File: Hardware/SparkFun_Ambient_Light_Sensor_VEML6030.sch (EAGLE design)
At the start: 25 parts, among them U1 VEML6030

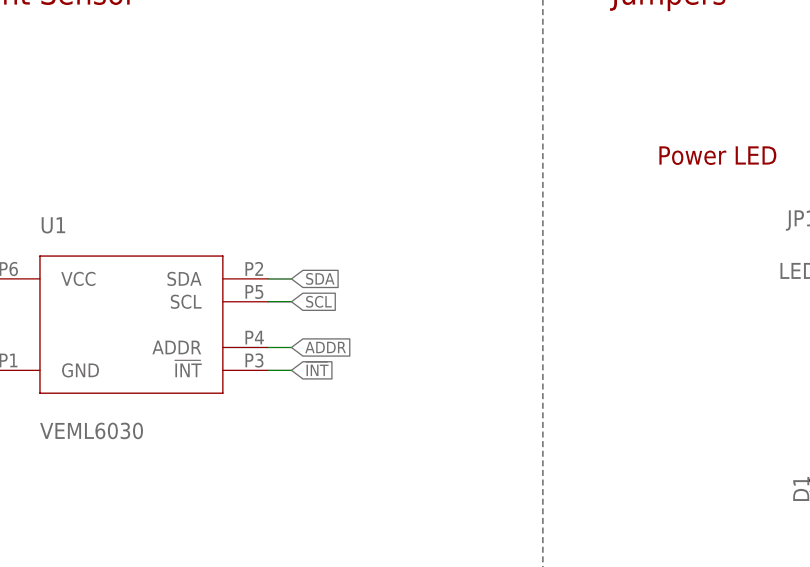
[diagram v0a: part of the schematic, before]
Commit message: Finishes tracework, adds 10k pull up resistor to interrupt pin, needs silk
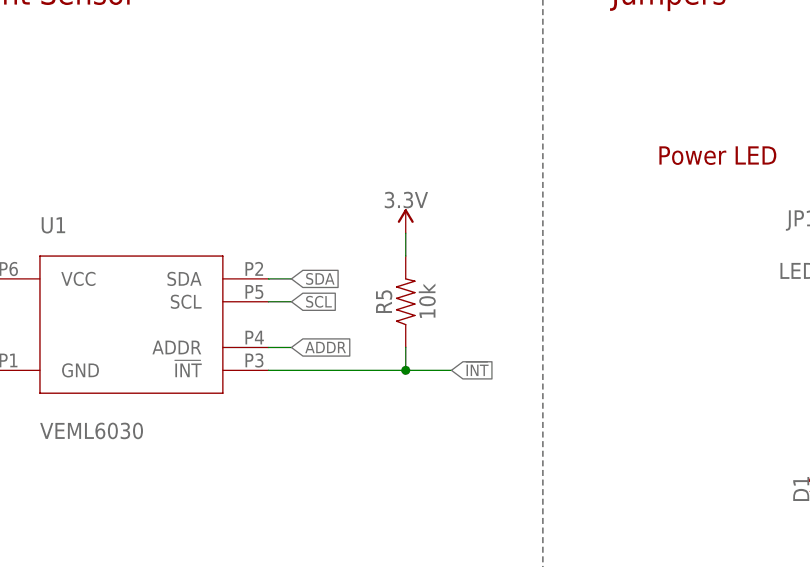
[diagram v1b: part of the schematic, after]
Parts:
- added R5: 10k, SparkFun-Resistors:10KOHM-0603-1/10W-1%
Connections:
- net !INT: now also R5.1
- net 3.3V: now also R5.2
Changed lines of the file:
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@@
 <part name="JP3" library="SparkFun-Jumpers" deviceset="JUMPER-SMT_3_2-NC_TRACE" device="_SILK" value="I2C_PU"/>
 <part name="SUPPLY7" library="SparkFun-PowerSymbols" deviceset="3.3V" device=""/>
+<part name="R5" library="SparkFun-Resistors" deviceset="10KOHM" device="-0603-1/10W-1%" value="10k"/>
+<part name="SUPPLY8" library="SparkFun-PowerSymbols" deviceset="3.3V" device=""/>
 </parts>
 <sheets>
@@
 <attribute name="VALUE" x="193.04" y="124.714" size="1.778" layer="96" align="bottom-center"/>
 </instance>
+<instance part="R5" gate="G$1" x="86.36" y="142.24" smashed="yes" rot="R90">
+<attribute name="NAME" x="84.836" y="142.24" size="1.778" layer="95" font="vector" rot="R90" align="bottom-center"/>
+<attribute name="VALUE" x="87.884" y="142.24" size="1.778" layer="96" font="vector" rot="R90" align="top-center"/>
+</instance>
+<instance part="SUPPLY8" gate="G$1" x="86.36" y="149.86" smashed="yes">
+<attribute name="VALUE" x="86.36" y="152.654" size="1.778" layer="96" align="bottom-center"/>
+</instance>
 </instances>
 <busses>
@@
 <wire x1="132.08" y1="83.82" x2="132.08" y2="86.36" width="0.1524" layer="91"/>
 </segment>
+<segment>
+<pinref part="R5" gate="G$1" pin="2"/>
+<wire x1="86.36" y1="147.32" x2="86.36" y2="149.86" width="0.1524" layer="91"/>
+<pinref part="SUPPLY8" gate="G$1" pin="3.3V"/>
+</segment>
 </net>
 <net name="GND" class="0">
@@
 <segment>
 <pinref part="U1" gate="G$1" pin="!INT"/>
-<wire x1="71.12" y1="134.62" x2="73.66" y2="134.62" width="0.1524" layer="91"/>
-<label x="73.66" y="134.62" size="1.27" layer="95" font="vector" xref="yes"/>
-</segment>
-<segment>
+<wire x1="71.12" y1="134.62" x2="86.36" y2="134.62" width="0.1524" layer="91"/>
+<label x="91.44" y="134.62" size="1.27" layer="95" font="vector" xref="yes"/>
+<pinref part="R5" gate="G$1" pin="1"/>
+<wire x1="86.36" y1="134.62" x2="91.44" y2="134.62" width="0.1524" layer="91"/>
+<wire x1="86.36" y1="137.16" x2="86.36" y2="134.62" width="0.1524" layer="91"/>
+<junction x="86.36" y="134.62"/>
+</segment>
+<segment>

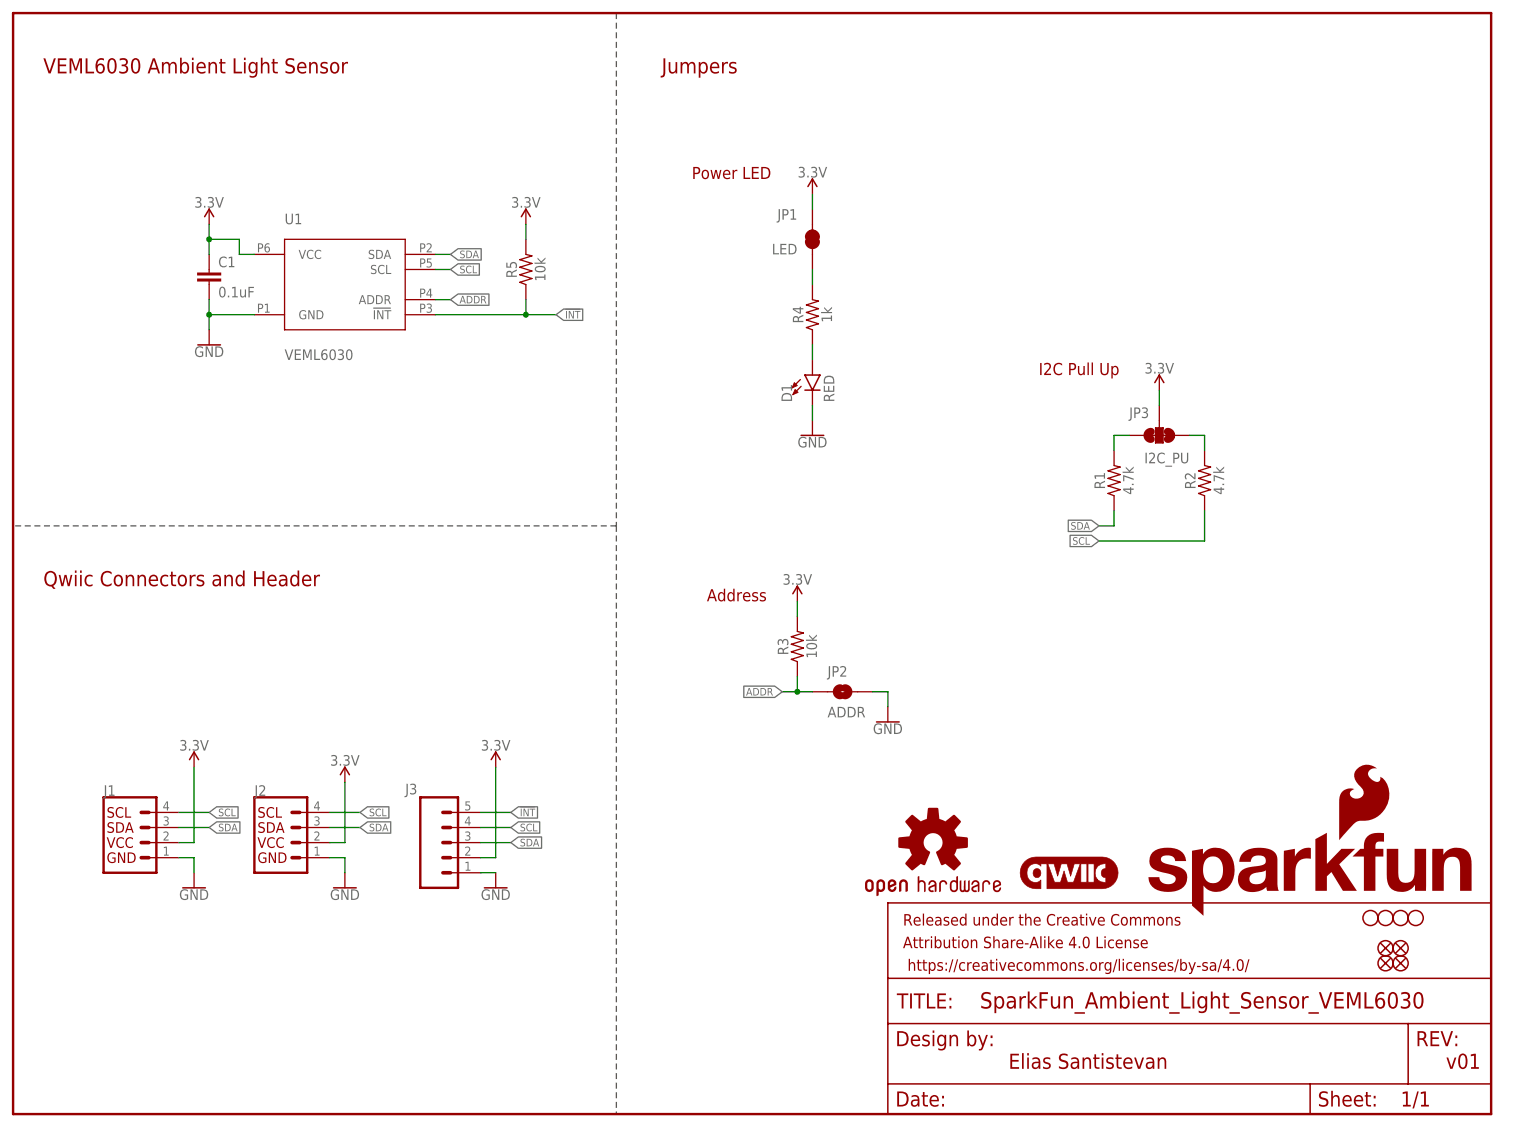
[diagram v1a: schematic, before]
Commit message: Adds silk to board for all things needing lables, adds text to jumpers in schematic,
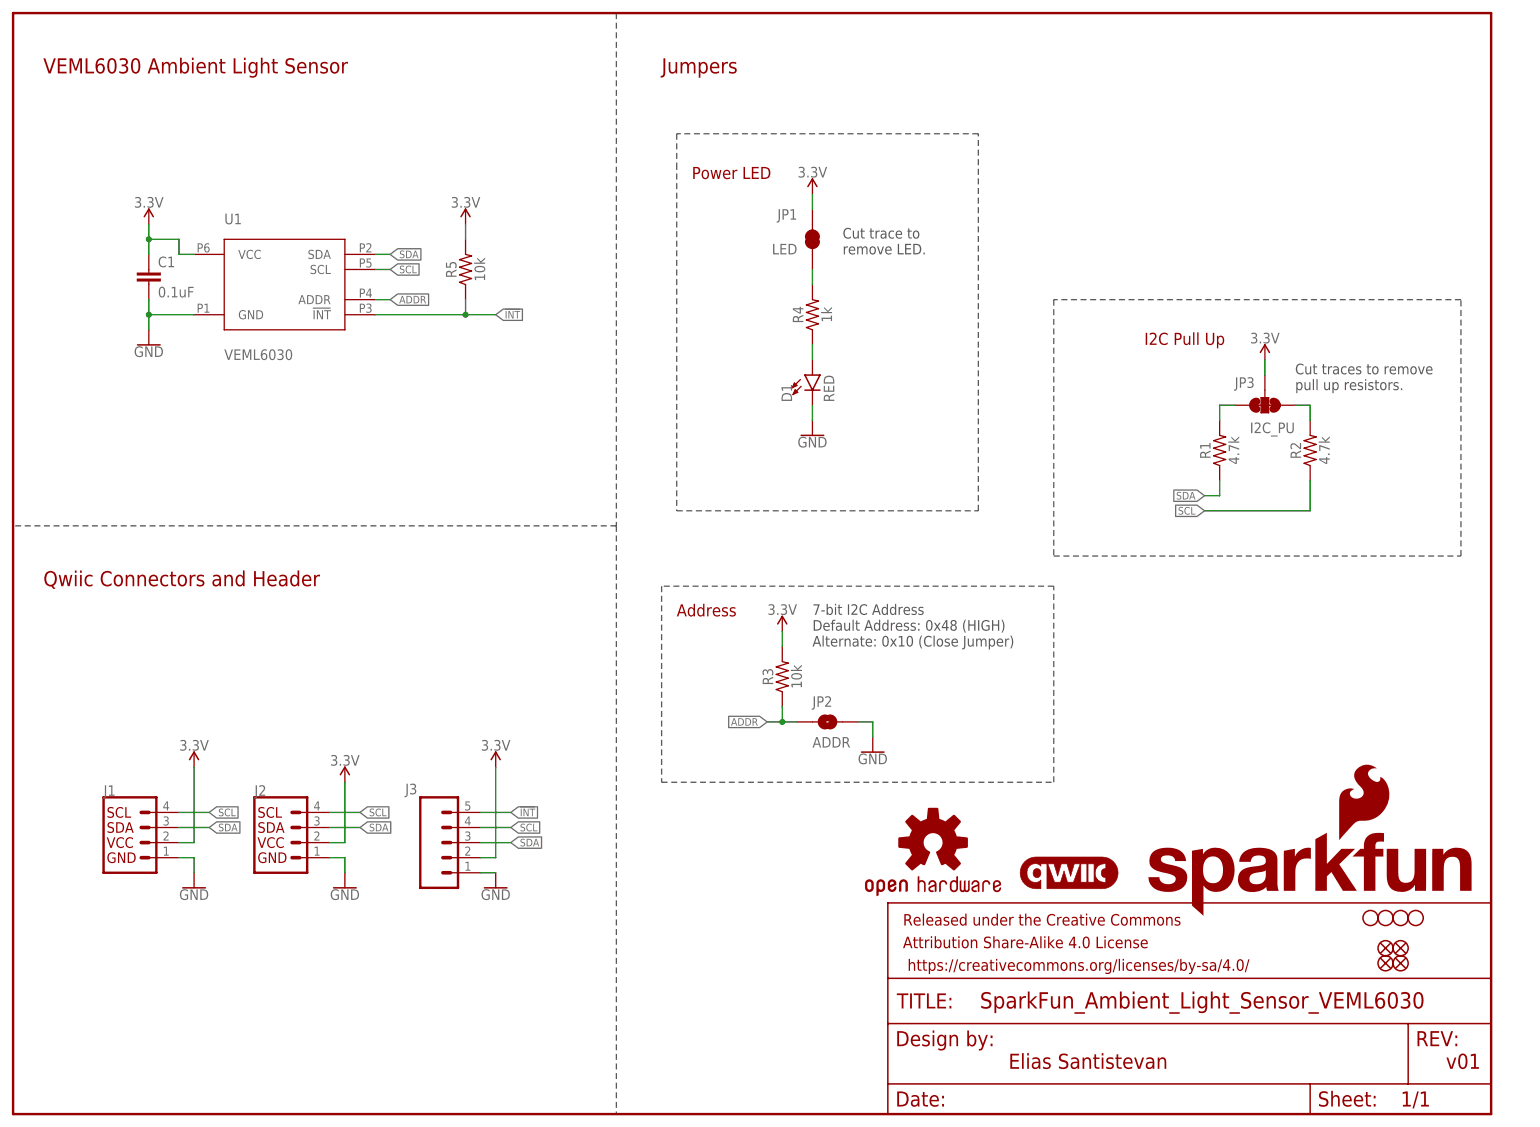
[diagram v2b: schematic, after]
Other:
- note added: "7-bit I2C Address Default Address: 0x48 (HIGH) Alternate: 0x10 (Close Jumper)"
- note added: "Cut trace to remove LED."
- note added: "Cut traces to remove pull up resistors."
- moved on the sheet: C1, JP2, JP3, R1, R2, R3, R5, U1

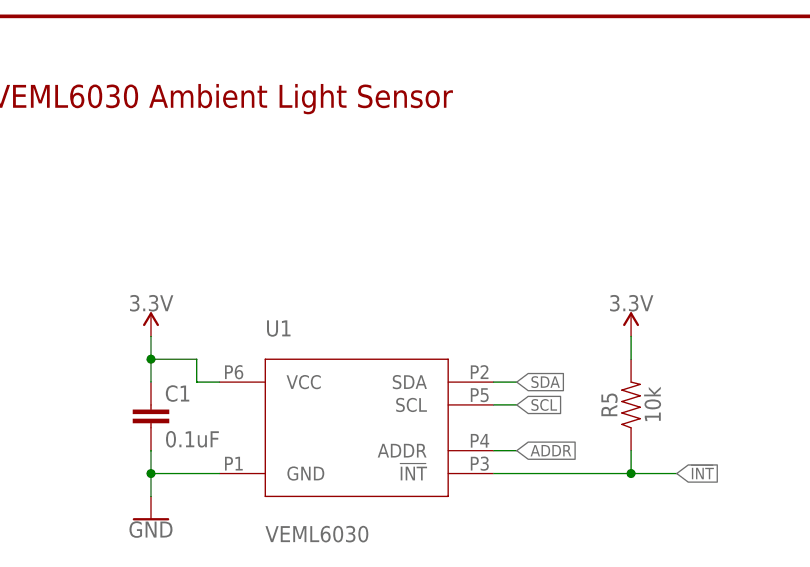
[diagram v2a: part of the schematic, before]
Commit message: Updates polarity marker on VEML6030, adds VCC range to schematic, improves ground pour on the underside.
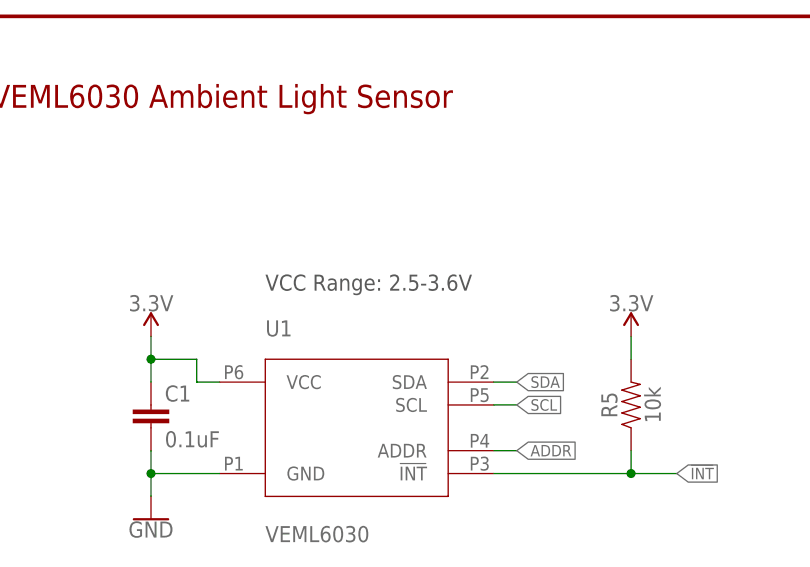
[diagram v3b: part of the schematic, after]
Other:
- note added: "VCC Range: 2.5-3.6V"
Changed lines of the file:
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@@
 <wire x1="243.84" y1="93.98" x2="243.84" y2="137.16" width="0.2032" layer="97" style="shortdash"/>
 <wire x1="243.84" y1="137.16" x2="175.26" y2="137.16" width="0.2032" layer="97" style="shortdash"/>
+<text x="35.56" y="154.94" size="1.778" layer="97" font="vector">VCC Range: 2.5-3.6V</text>
 </plain>
 <instances>
